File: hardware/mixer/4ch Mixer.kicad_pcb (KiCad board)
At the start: 2 copper layers, 30 x 100 mm, 60 parts, among them P1 Power, U1 TL074, U2 TL072

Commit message: Main PCB: harmonize branding text with the Multiple's pattern
Reformatted the combined "Quad Mixer\nV1.0\nschenktronics.com" to
"ST-04 v1.0\nQuad Mixer\nschenktronics.com" (code + version leading,
matching the other boards' convention). Kept it on the front where it
already had a clear, proven spot -- tried moving it to the back to
match the Multiple/Attenuverter/Attenuator convention, but this board's
back is routed edge to edge with no clear pocket that size; moving it
there just put it on top of real traces. Logo (medium S-mark) unchanged.

Also tried adding the CC BY-NC-SA roundels, same result as the
Attenuverter -- no space without overlapping copper, left off.
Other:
- board text added: "ST-04 v1.0 Quad Mixer schenktronics.com"
- board text removed: "Quad Mixer V1.0 schenktronics.com"
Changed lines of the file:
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@@
 		(layer "Edge.Cuts")
 	)
-	(gr_text "Quad Mixer\nV1.0\nschenktronics.com"
+	(gr_text "ST-04 v1.0\nQuad Mixer\nschenktronics.com"
 		(at 101.6 95 0)
 		(layer "F.SilkS")

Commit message: Main PCB: hand-placed branding text on the back, add CC license text
Nathan's own edit in KiCad: moved the ST-04/Quad Mixer text from the
front to a clear spot on the back, and added "CC BY-NC-SA 4.0" text
(matching the other boards -- text only, no icon roundels).
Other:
- board text added: "CC BY-NC-SA 4.0"
- board text added: "ST-04 v1.0 Quad Mixer"
- board text added: "schenktronics.com"
- board text removed: "ST-04 v1.0 Quad Mixer schenktronics.com"
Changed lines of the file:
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@@
 		(layer "Edge.Cuts")
-	)
-	(gr_text "ST-04 v1.0\nQuad Mixer\nschenktronics.com"
-		(at 101.6 95 0)
-		(layer "F.SilkS")
-		(effects
-			(font
-				(size 1 1)
-				(thickness 0.15)
-			)
-			(justify left bottom)
-		)
 	)
 	(gr_text "-12V"
@@
 		)
 	)
+	(gr_text "ST-04 v1.0\nQuad Mixer"
+		(at 124.2 53.8 0)
+		(layer "B.SilkS")
+		(effects
+			(font
+				(size 1 1)
+				(thickness 0.15)
+			)
+			(justify left bottom mirror)
+		)
+	)
 	(gr_text "+12V"
 		(at 129.6 114.6 0)
@@
 		)
 	)
+	(gr_text "CC BY-NC-SA 4.0"
+		(at 100.6 117.6 270)
+		(layer "B.SilkS")
+		(effects
+			(font
+				(size 1 1)
+				(thickness 0.15)
+			)
+			(justify left bottom mirror)
+		)
+	)
+	(gr_text "schenktronics.com"
+		(at 100.8 87.6 270)
+		(layer "B.SilkS")
+		(effects
+			(font
+				(size 1 1)
+				(thickness 0.15)
+			)
+			(justify left bottom mirror)
+		)
+	)
 	(gr_text "Red Stripe"
 		(at 115.4 114.6 270)
@@
 	)
 	(segment
+		(start 119.647 142.43)
+		(end 117.077 145)
+		(width 0.25)
+		(layer "B.Cu")
+		(net "Net-(J5-PadT)")
+	)
+	(segment
+		(start 119.647 140.4)
+		(end 119.647 142.43)
+		(width 0.25)
+		(layer "B.Cu")
+		(net "Net-(J5-PadT)")
+	)
+	(segment
 		(start 111.7555 143.7555)
 		(end 113 145)
@@
 	)
 	(segment
-		(start 119.647 142.43)
-		(end 117.077 145)
-		(width 0.25)
-		(layer "B.Cu")
-		(net "Net-(J5-PadT)")
-	)
-	(segment
-		(start 119.647 140.4)
-		(end 119.647 142.43)
-		(width 0.25)
-		(layer "B.Cu")
-		(net "Net-(J5-PadT)")
-	)
-	(segment

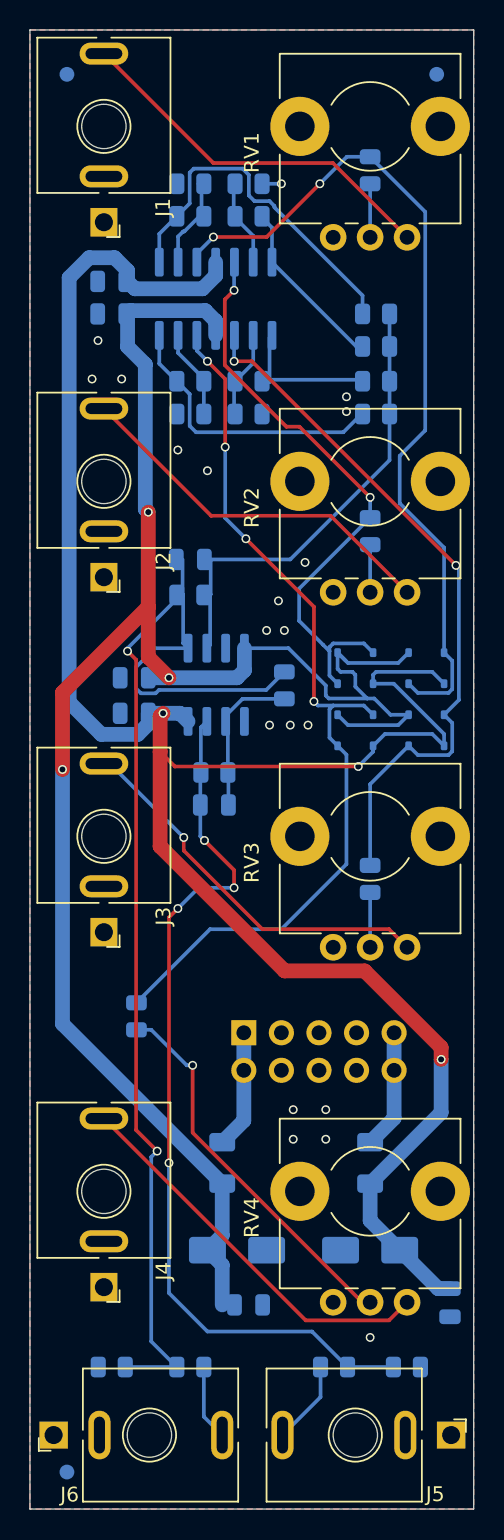
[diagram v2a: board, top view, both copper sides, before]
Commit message: Fix library reference, add 3d models
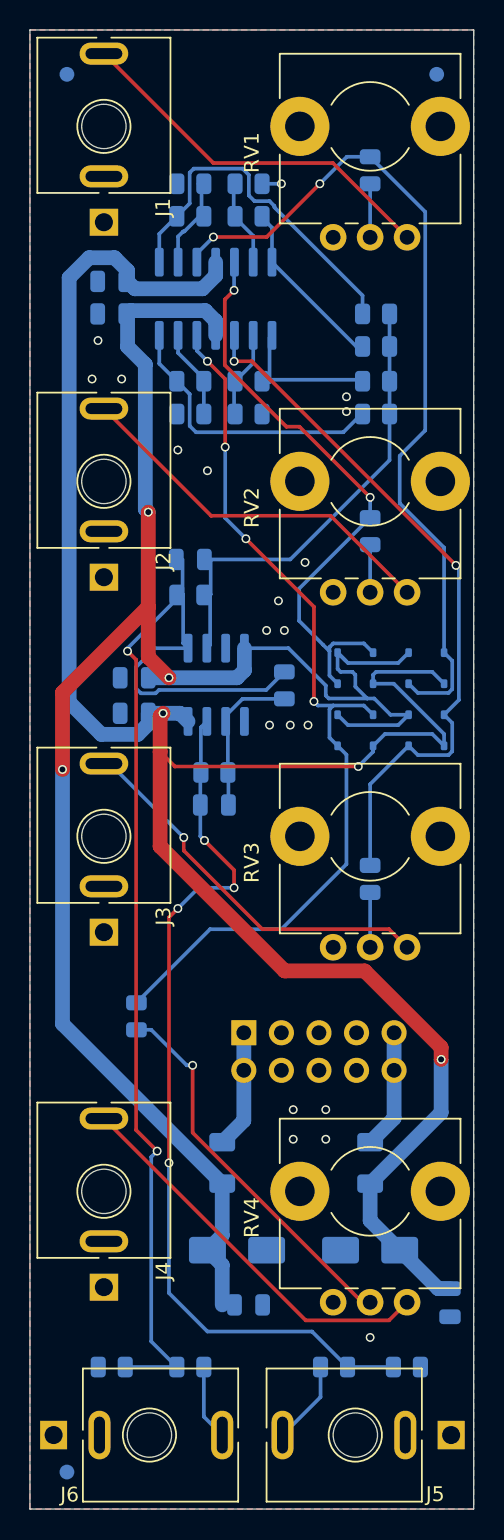
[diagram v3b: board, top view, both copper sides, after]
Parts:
- FID1, FID2, FID3: footprint Fiducial_1mm_Mask2mm -> Fiducial:Fiducial_1mm_Mask2mm
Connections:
- RV1 pad : (no net) -> GNDA
- RV2 pad : (no net) -> GNDA
- RV3 pad : (no net) -> GNDA
- RV4 pad : (no net) -> GNDA

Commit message: Drop channel gain to ×1, swap pots to 100k, add STEP-based outline drawings
Each channel's op-amp (U1) was wired for ×2 gain, with the pot giving
0-2x overall and unity at its center click. Changed R5-R8 (feedback
resistors) from 10k to 0R, making each stage a unity-gain buffer, so
the range is now 0-1x with no gain above the input's own level. R1-R4
stay at 10k; reverting a channel to ×2 just needs its R5-R8 swapped
back to 10k. This also raises per-channel clipping headroom from
±5V to the full ±10V op-amp swing, since nothing is thrown away by a
later attenuation stage. Updated the manual, assembly guide, README,
BOM/manufacturing CSVs and the generated panel/patch drawings to
match.

Also switches RV1-RV4 from the substituted 10k pot to the originally-
specced Bourns 100k pot (no center detent), removes now-stale detent
language repo-wide, and wires in real STEP-based outline drawings
(replacing product photos in the README/manual/assembly guide).
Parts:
- R5, R6, R7, R8: value 10k -> 0
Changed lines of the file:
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@@
 			)
 		)
-		(property "Value" "10k"
+		(property "Value" "0"
 			(at 0 -1.65 180)
 			(layer "B.Fab")
@@
 			)
 		)
-		(property "Value" "10k"
+		(property "Value" "0"
 			(at 0 -1.65 0)
 			(layer "B.Fab")
@@
 			)
 		)
-		(property "Value" "10k"
+		(property "Value" "0"
 			(at 0 -1.65 0)
 			(layer "B.Fab")
@@
 			)
 		)
-		(property "Value" "10k"
+		(property "Value" "0"
 			(at 0 -1.65 180)
 			(layer "B.Fab")
